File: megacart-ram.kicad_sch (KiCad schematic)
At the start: 14 parts, among them J1 Conn_02x08_Counter_Clockwise, U1 AS6C4008-55PCN, U10 7432, U11 7432, U12 74LS138, U2 74HC273, U3 74HC74, U4 7421, U5 7421, U6 7402, U7 74HC04, U8 7408, U9 7408

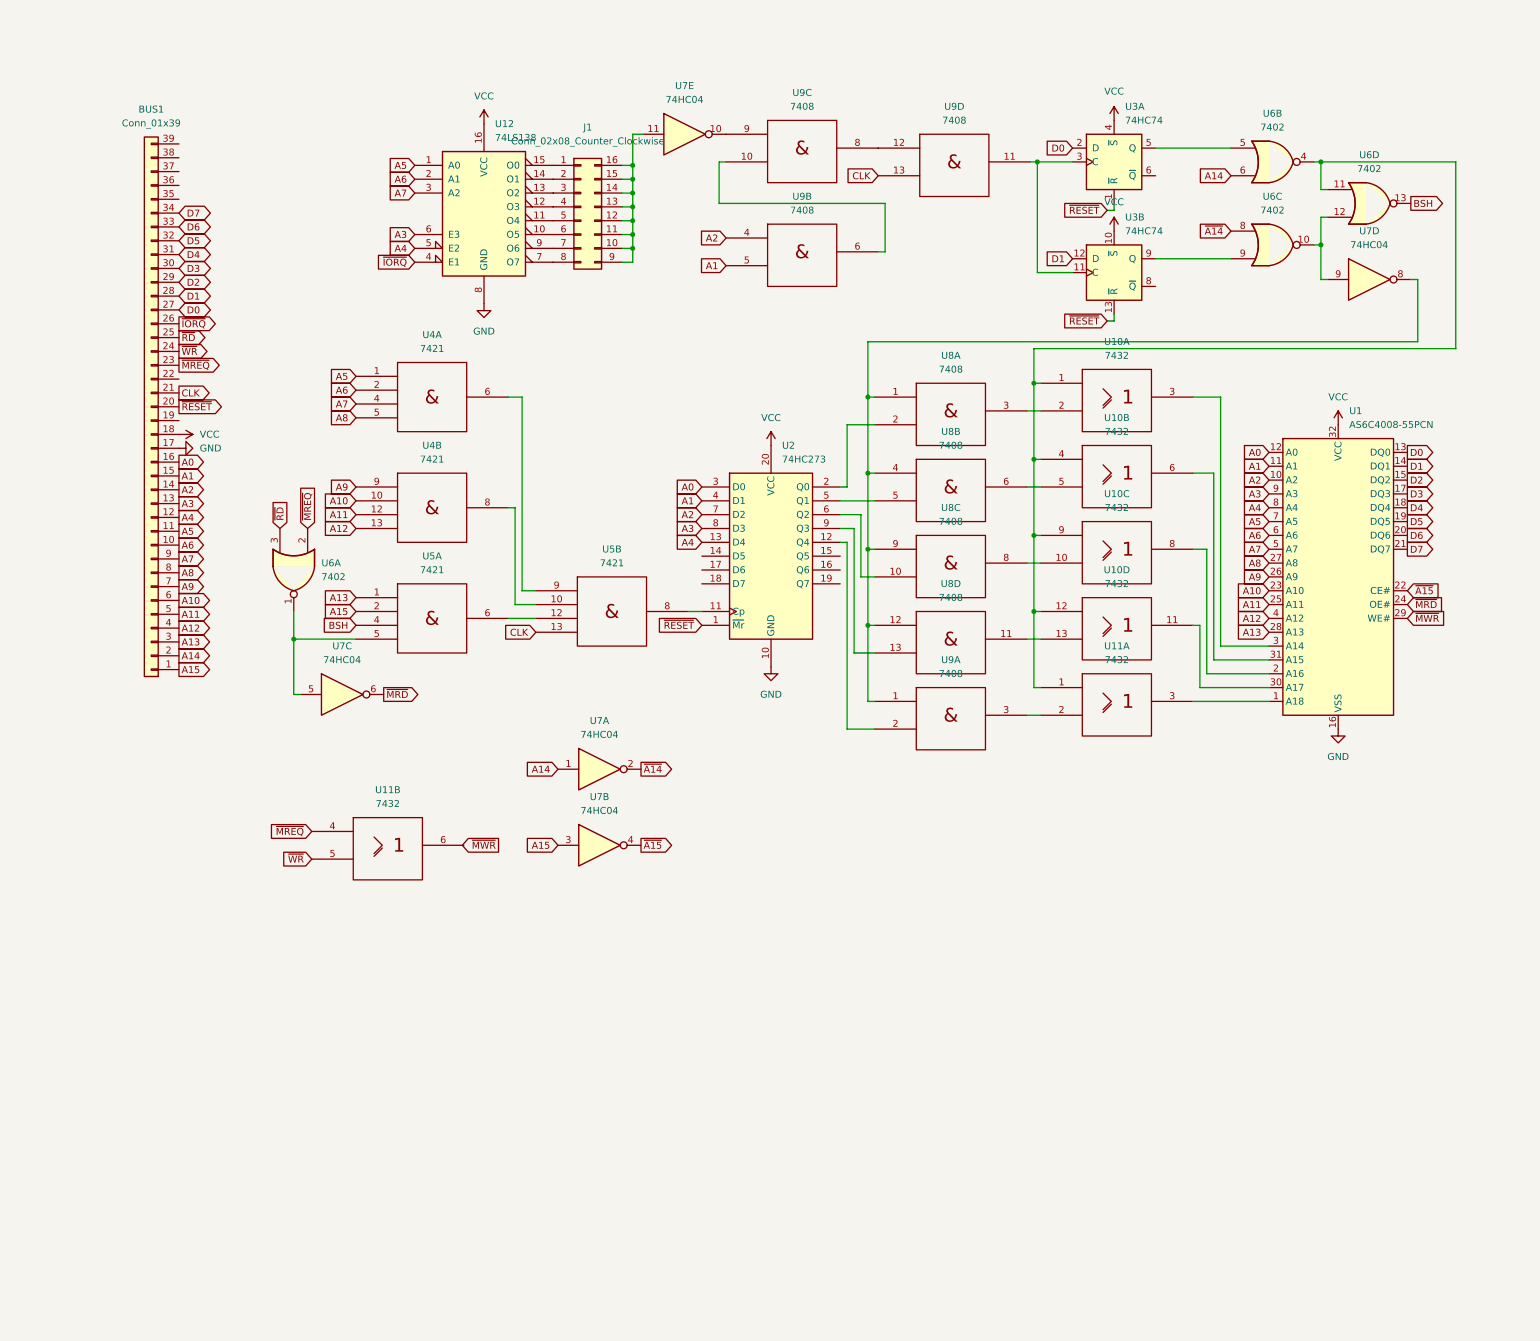
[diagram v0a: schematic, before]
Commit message: Clean up schematic.
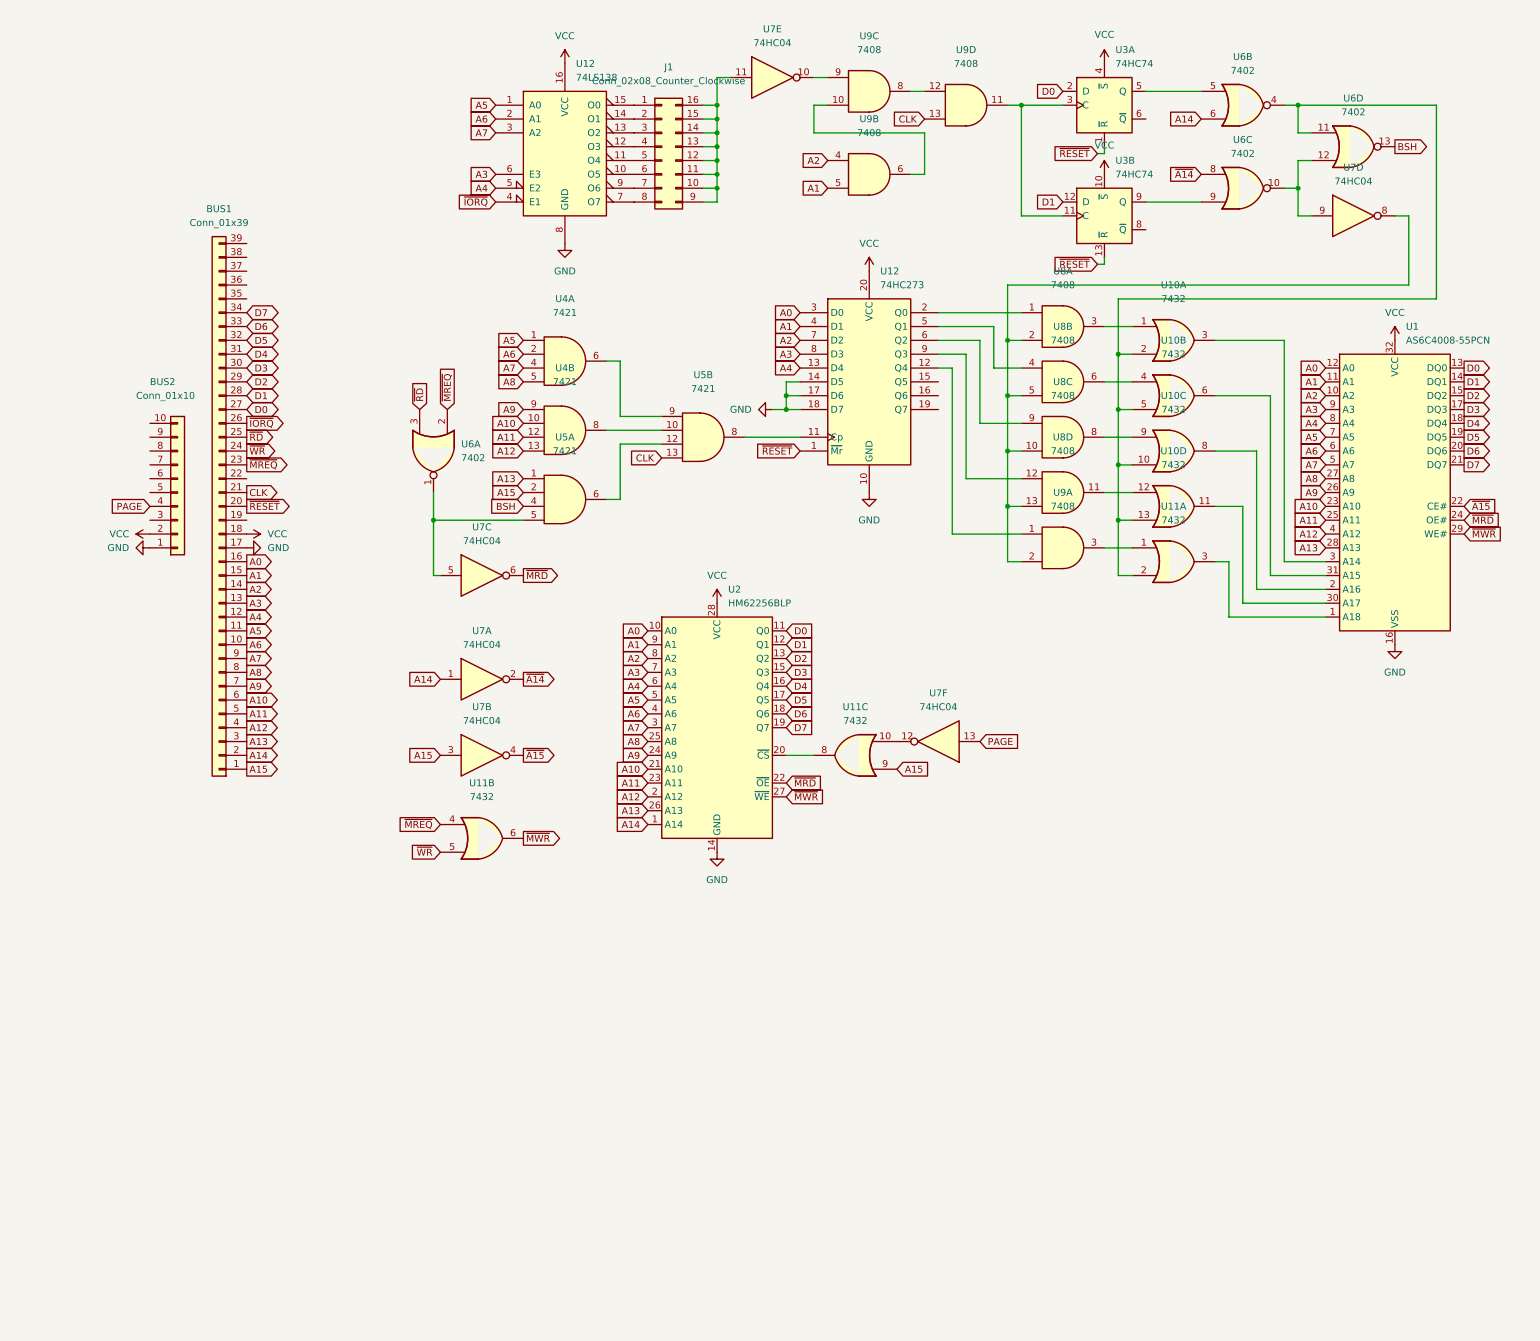
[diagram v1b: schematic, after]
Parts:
- added BUS2: Conn_01x10, symbol Connector_Generic:Conn_01x10
- added unit 3 of U11
- added U2: HM62256BLP, Package_DIP:DIP-28_W15.24mm, symbol Memory_RAM:HM62256BLP
- added unit 6 of U7
- U10, U11: symbol 74xx_IEEE:7432 -> 74xx:74LS32
- U4, U5: symbol 74xx_IEEE:7421 -> 74xx:74LS21
- U8, U9: symbol 74xx_IEEE:7408 -> 74xx:74LS08
- renumbered U2 to U12
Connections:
- net A0: now also U2.10 (A0)
- net A1: now also U2.9 (A1)
- net A10: now also U2.21 (A10)
- net A11: now also U2.23 (A11)
- net A12: now also U2.2 (A12)
- net A13: now also U2.26 (A13)
- net A14: now also U2.1 (A14)
- net A15: now also U11.9
- net A2: now also U2.8 (A2)
- net A3: now also U2.7 (A3)
- net A4: now also U2.6 (A4)
- net A5: now also U2.5 (A5)
- net A6: now also U2.4 (A6)
- net A7: now also U2.3 (A7)
- net A8: now also U2.25 (A8)
- net A9: now also U2.24 (A9)
- net D0: now also U2.11 (Q0)
- net D1: now also U2.12 (Q1)
- net D2: now also U2.13 (Q2)
- net D3: now also U2.15 (Q3)
- net D4: now also U2.16 (Q4)
- net D5: now also U2.17 (Q5)
- net D6: now also U2.18 (Q6)
- net D7: now also U2.19 (Q7)
- net GND: now also U12.14 (D5), U12.17 (D6), U12.18 (D7), BUS2.1 (Pin_1), U2.14 (GND)
- net VCC: now also BUS2.2 (Pin_2), U2.28 (VCC)
- net ~{MRD}: now also U2.22 (~{OE})
- net ~{MWR}: now also U11.6, U2.27 (~{WE})
- net at U12.12 (Q4): now also U9.1; no longer U9.2
- net at U12.2 (Q0): now also U8.1; no longer U8.2
- net at U12.5 (Q1): now also U8.4; no longer U8.5
- net at U12.6 (Q2): now also U8.9; no longer U8.10
- net at U12.9 (Q3): now also U8.12; no longer U8.13
- net at U10.10: now also U10.13, U10.2, U10.5, U11.2, U6.11, U6.4; no longer U8.8
- net at U8.11: now also U10.12; no longer U10.13
- net at U9.3: now also U11.1; no longer U11.2
- net at U8.3: now also U10.1; no longer U10.2
- net at U8.6: now also U10.4; no longer U10.5
- removed net Gnd: U10.7 (Gnd), U10.7 (Gnd), U10.7 (Gnd), U10.7 (Gnd), U11.7 (Gnd), U11.7 (Gnd), U4.7 (Gnd), U4.7 (Gnd), U5.7 (Gnd), U5.7 (Gnd), U8.7 (Gnd), U8.7 (Gnd), U8.7 (Gnd), U8.7 (Gnd), U9.7 (Gnd), U9.7 (Gnd), U9.7 (Gnd), U9.7 (Gnd)
- removed net Vcc: U10.14 (Vcc), U10.14 (Vcc), U10.14 (Vcc), U10.14 (Vcc), U11.14 (Vcc), U11.14 (Vcc), U4.14 (Vcc), U4.14 (Vcc), U5.14 (Vcc), U5.14 (Vcc), U8.14 (Vcc), U8.14 (Vcc), U8.14 (Vcc), U8.14 (Vcc), U9.14 (Vcc), U9.14 (Vcc), U9.14 (Vcc), U9.14 (Vcc)
- new net: U10.9, U8.8
- new net: U11.8, U2.20 (~{CS})
- new net: U7.8, U8.10, U8.13, U8.2, U8.5, U9.2
- new net: U11.10, U7.12
- new net PAGE: BUS2.4 (Pin_4), U7.13
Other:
- moved on the sheet: BUS1, J1, U1, U12, U3A, U3B, U6A, U6B, U6C, U6D, U7A, U7B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

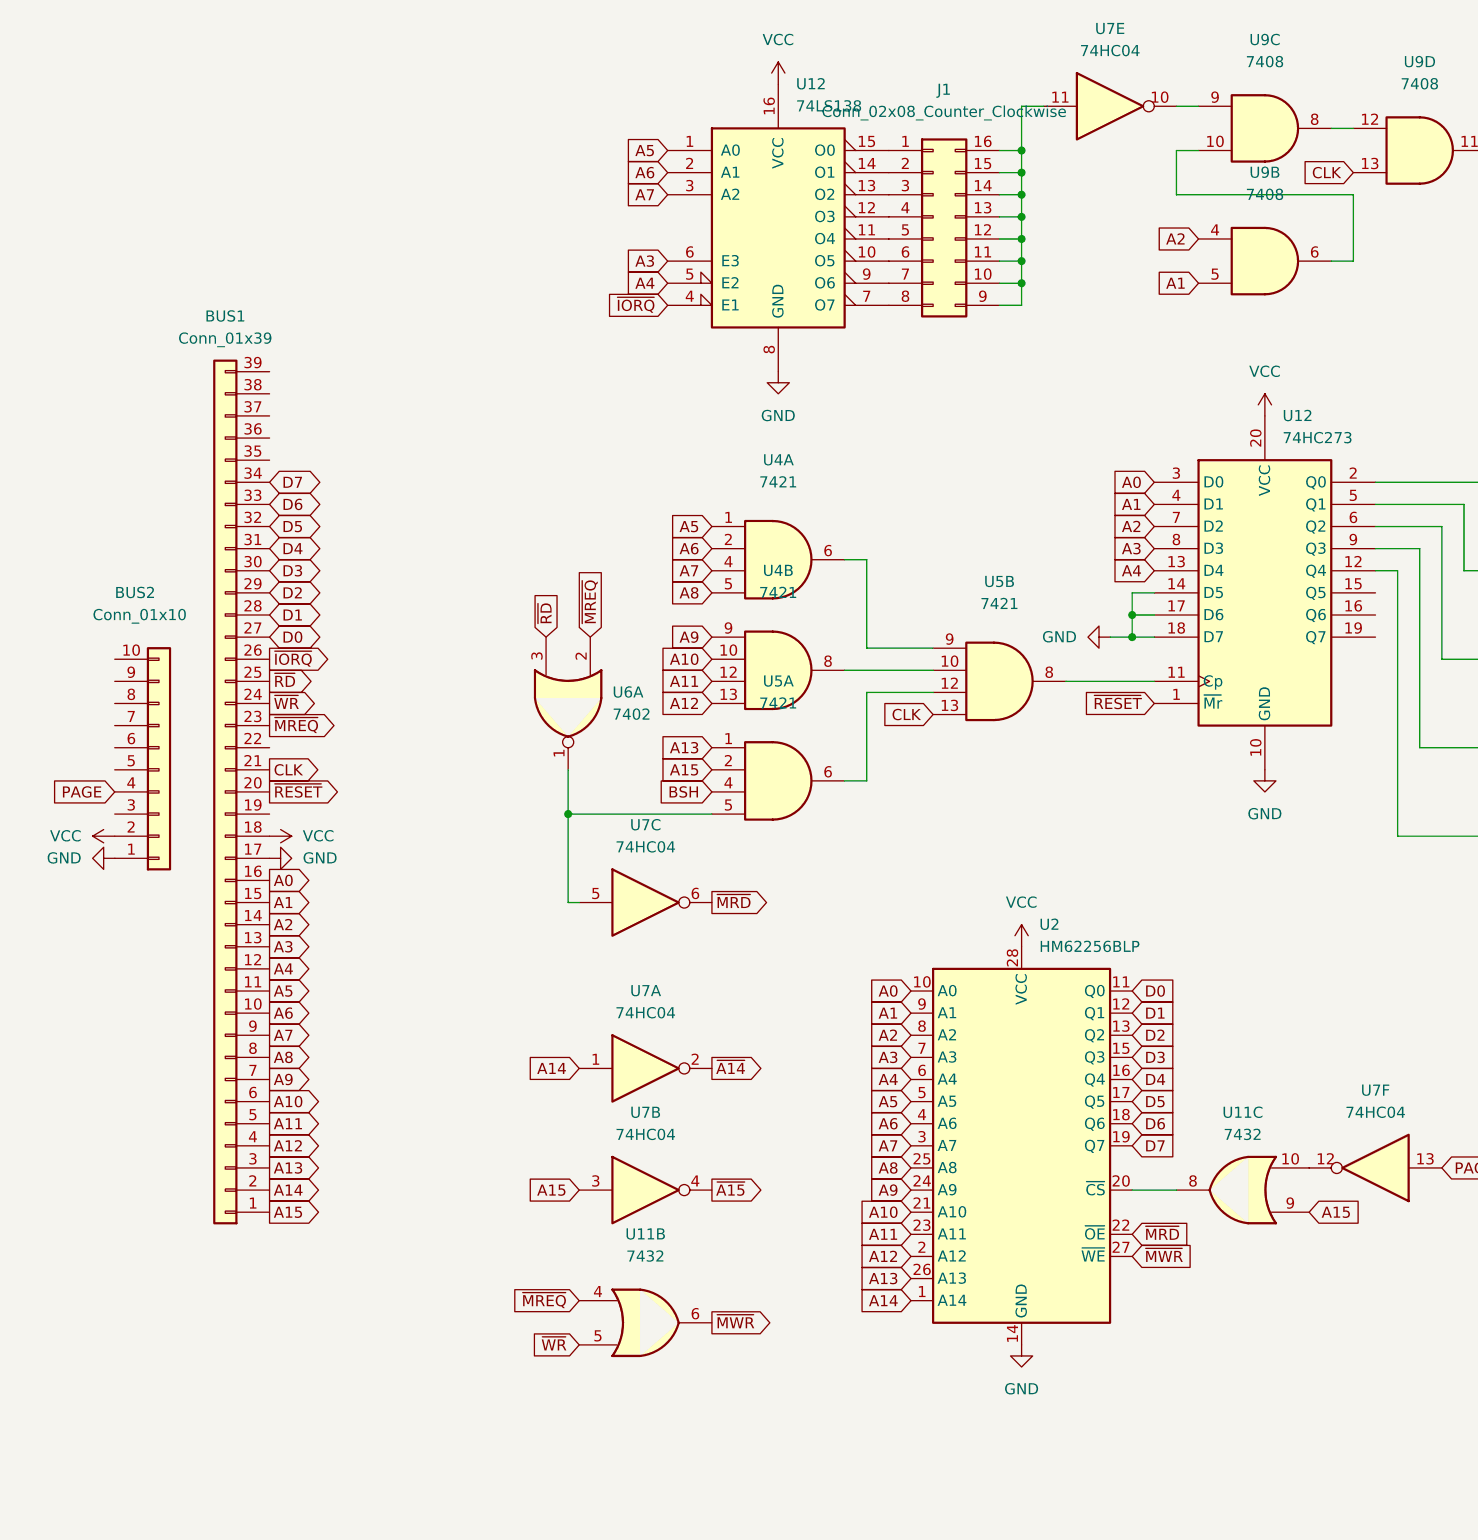
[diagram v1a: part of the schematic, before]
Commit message: Add decoupling caps and update PCB with RC2014 template.
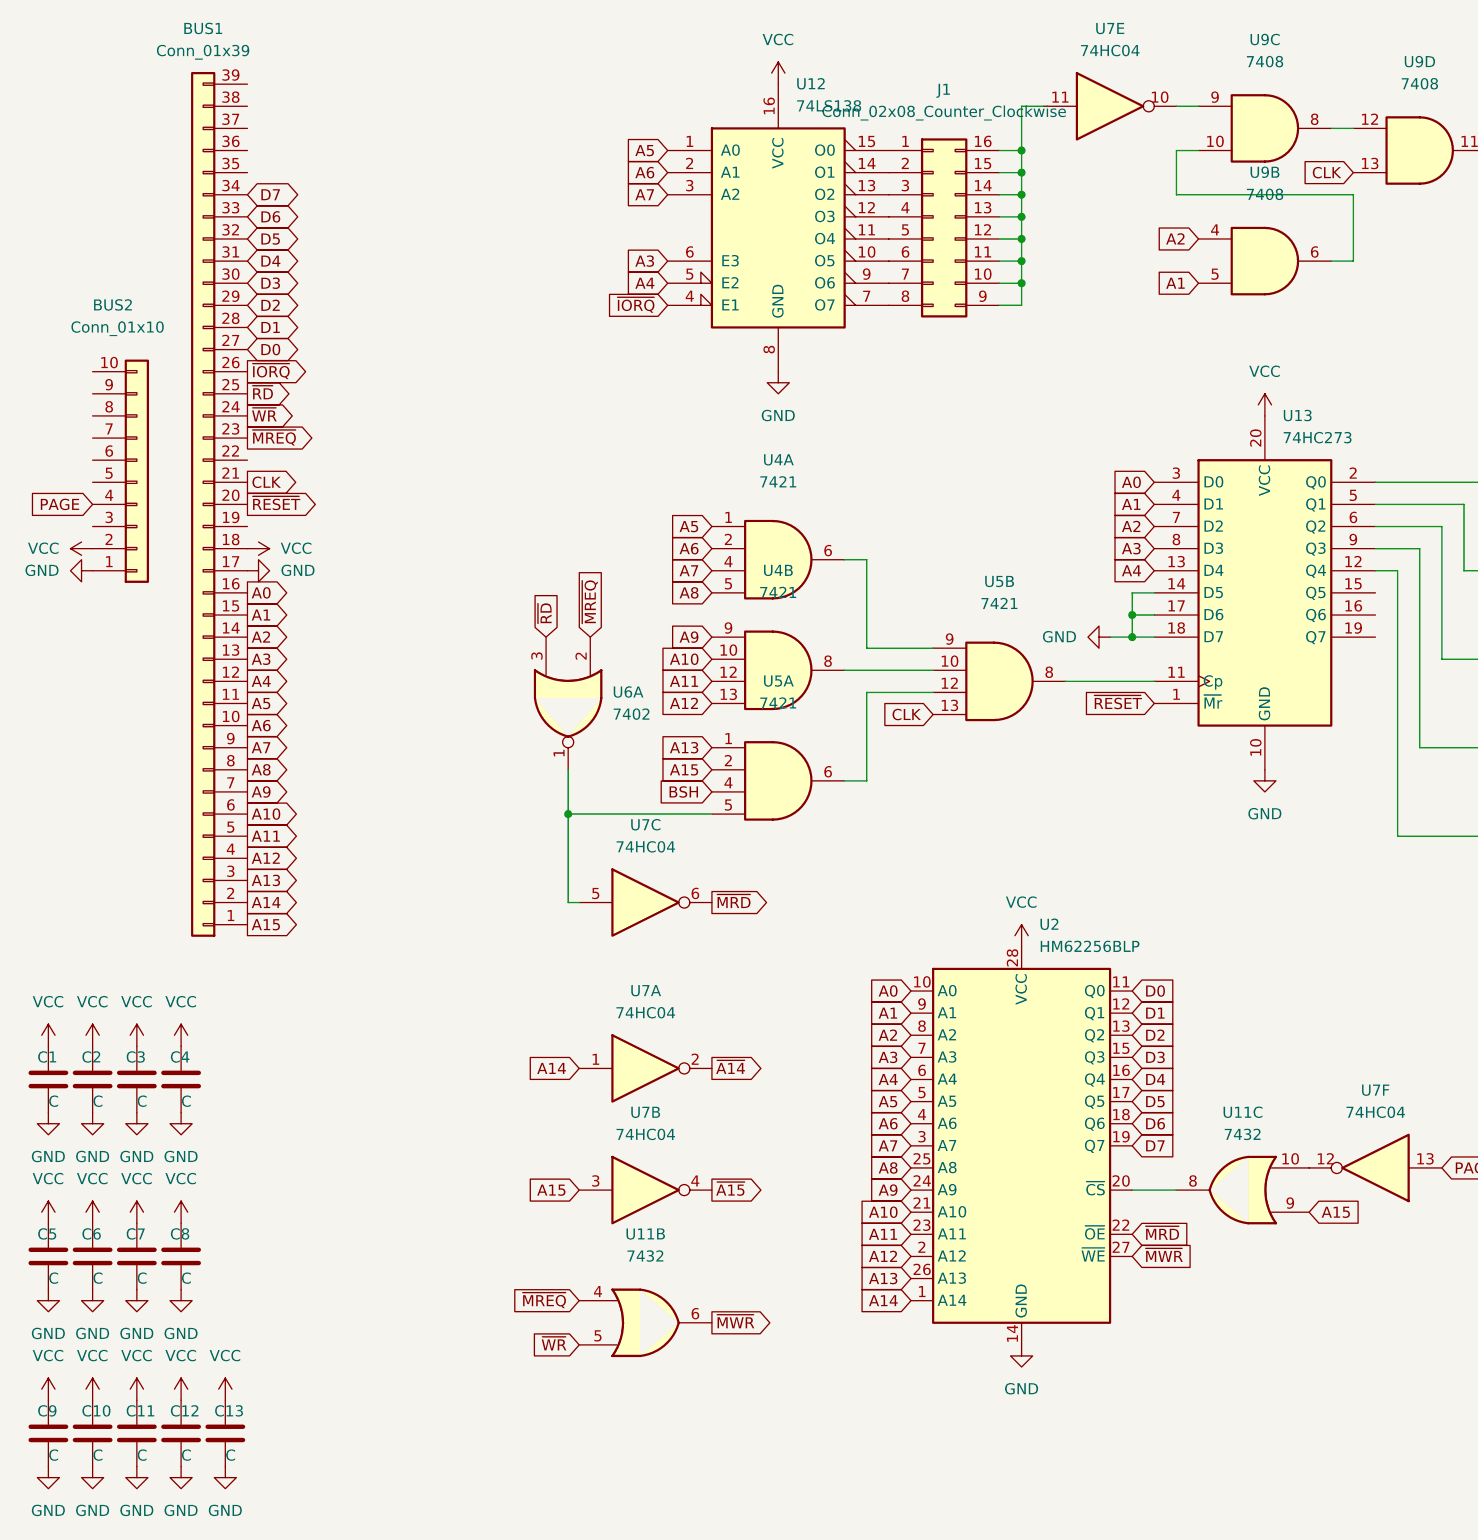
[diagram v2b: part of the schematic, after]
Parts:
- added C1, C10, C11, C12, C13, C2, C3, C4, C5, C6, C7, C8, C9: C, Capacitor_THT:C_Disc_D5.0mm_W2.5mm_P2.50mm, symbol Device:C
- BUS2: footprint (none) -> Connector_PinHeader_2.54mm:PinHeader_1x10_P2.54mm_Vertical
- renumbered U12 to U13
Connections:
- net GND: now also C1.2, C10.2, C11.2, C12.2, C13.2, C2.2, C3.2, C4.2, C5.2, C6.2, C7.2, C8.2, C9.2
- net VCC: now also C1.1, C10.1, C11.1, C12.1, C13.1, C2.1, C3.1, C4.1, C5.1, C6.1, C7.1, C8.1, C9.1
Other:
- moved on the sheet: BUS1, BUS2
